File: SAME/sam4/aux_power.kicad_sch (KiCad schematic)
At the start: 13 parts, among them J10 Conn_02x02_Odd_Even, J12 S2B-EH, J20 S2B-EH, J21 S2B-EH, J22 S2B-EH, U10 D36V50F5, U11 D36V50F12

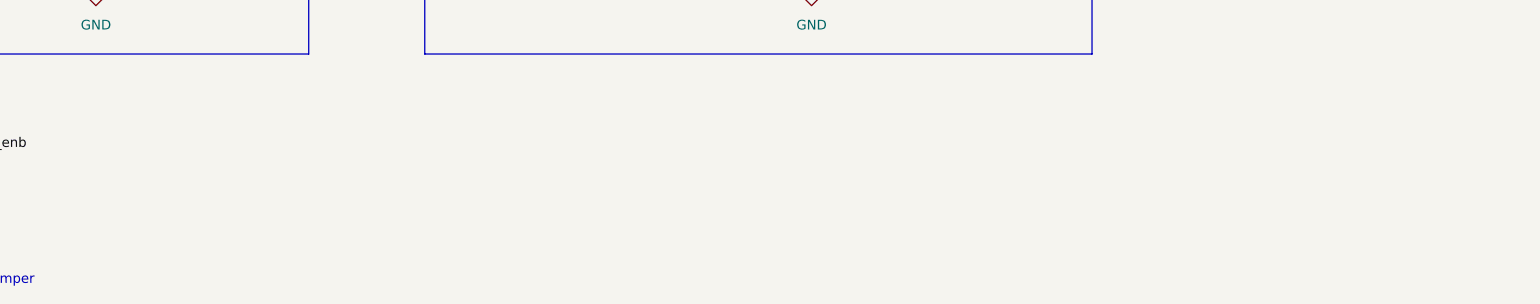
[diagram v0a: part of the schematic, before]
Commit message: final san check routing. add protection
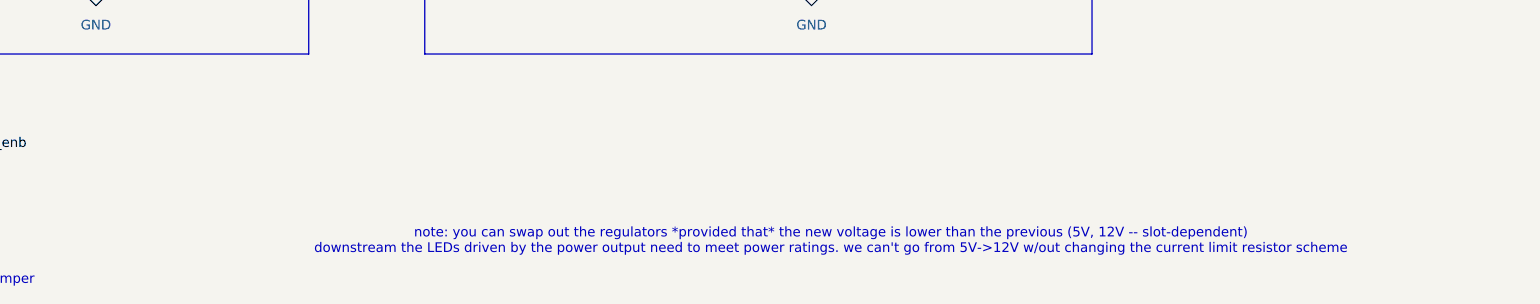
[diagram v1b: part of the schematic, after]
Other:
- note added: "note: you can swap out the regulators *provided that* the new voltage is lower than the previous (5V, 12V -- slot-dependent) downstream the LEDs driven by the power output need to meet power ratings. we can't go from 5V->12V w/out changing the current limit resistor scheme"
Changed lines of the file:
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@@
+		)
+	)
+	(text "note: you can swap out the regulators *provided that* the new voltage is lower than the previous (5V, 12V -- slot-dependent)\ndownstream the LEDs driven by the power output need to meet power ratings. we can't go from 5V->12V w/out changing the current limit resistor scheme"
+		(exclude_from_sim no)
+		(at 175.26 132.588 0)
+		(effects
+			(font
+				(size 1.27 1.27)
+			)
 		)
 	)

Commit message: add JLC ordering files. small tweaks
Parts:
- J12, J20, J21, J22: LCSC (none) -> C514173
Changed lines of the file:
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@@
 			)
 		)
-		(property "LCSC" ""
+		(property "LCSC" "C514173"
 			(at 87.63 91.44 0)
 			(effects
@@
 			)
 		)
-		(property "LCSC" ""
+		(property "LCSC" "C514173"
 			(at 87.63 97.79 0)
 			(effects
@@
 			)
 		)
-		(property "LCSC" ""
+		(property "LCSC" "C514173"
 			(at 181.61 91.44 0)
 			(effects
@@
 			)
 		)
-		(property "LCSC" ""
+		(property "LCSC" "C514173"
 			(at 181.61 97.79 0)
 			(effects

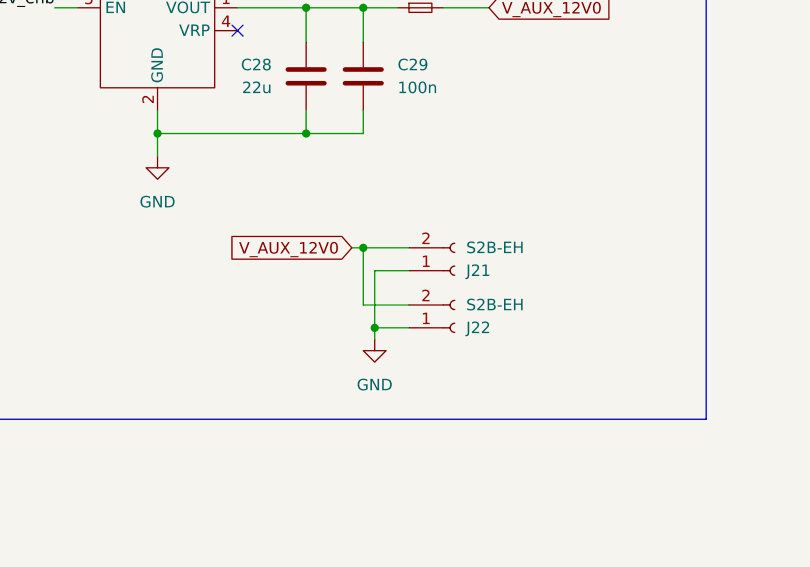
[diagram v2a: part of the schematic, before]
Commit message: update SAME connectors to better fit SAME mechanical design
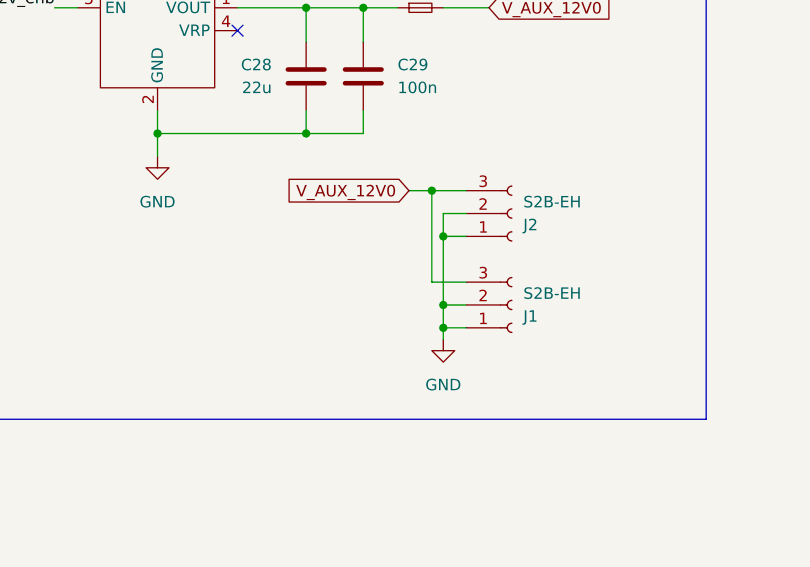
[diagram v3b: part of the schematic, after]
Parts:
- removed J21, J22: S2B-EH, Connector_JST:JST_EH_S2B-EH_1x02_P2.50mm_Horizontal, symbol Connector:Conn_01x02_Socket
- added J1, J2: S2B-EH, Connector_JST:JST_EH_S3B-EH_1x03_P2.50mm_Horizontal, symbol Connector:Conn_01x03_Socket
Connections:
- net GND: now also J1.1 (Pin_1), J1.2 (Pin_2), J2.1 (Pin_1), J2.2 (Pin_2)
- net V_AUX_12V0: now also J1.3 (Pin_3), J2.3 (Pin_3)
